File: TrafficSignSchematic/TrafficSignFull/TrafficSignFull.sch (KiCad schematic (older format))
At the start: 36 parts, among them J1 LED matrix data, J2 LED matrix power, J3 Power input, SW1 Power switch, U1 ATmega328P-PU, U2 SIM800L, U3 BQ24650 charge controller, Y1 16MHz

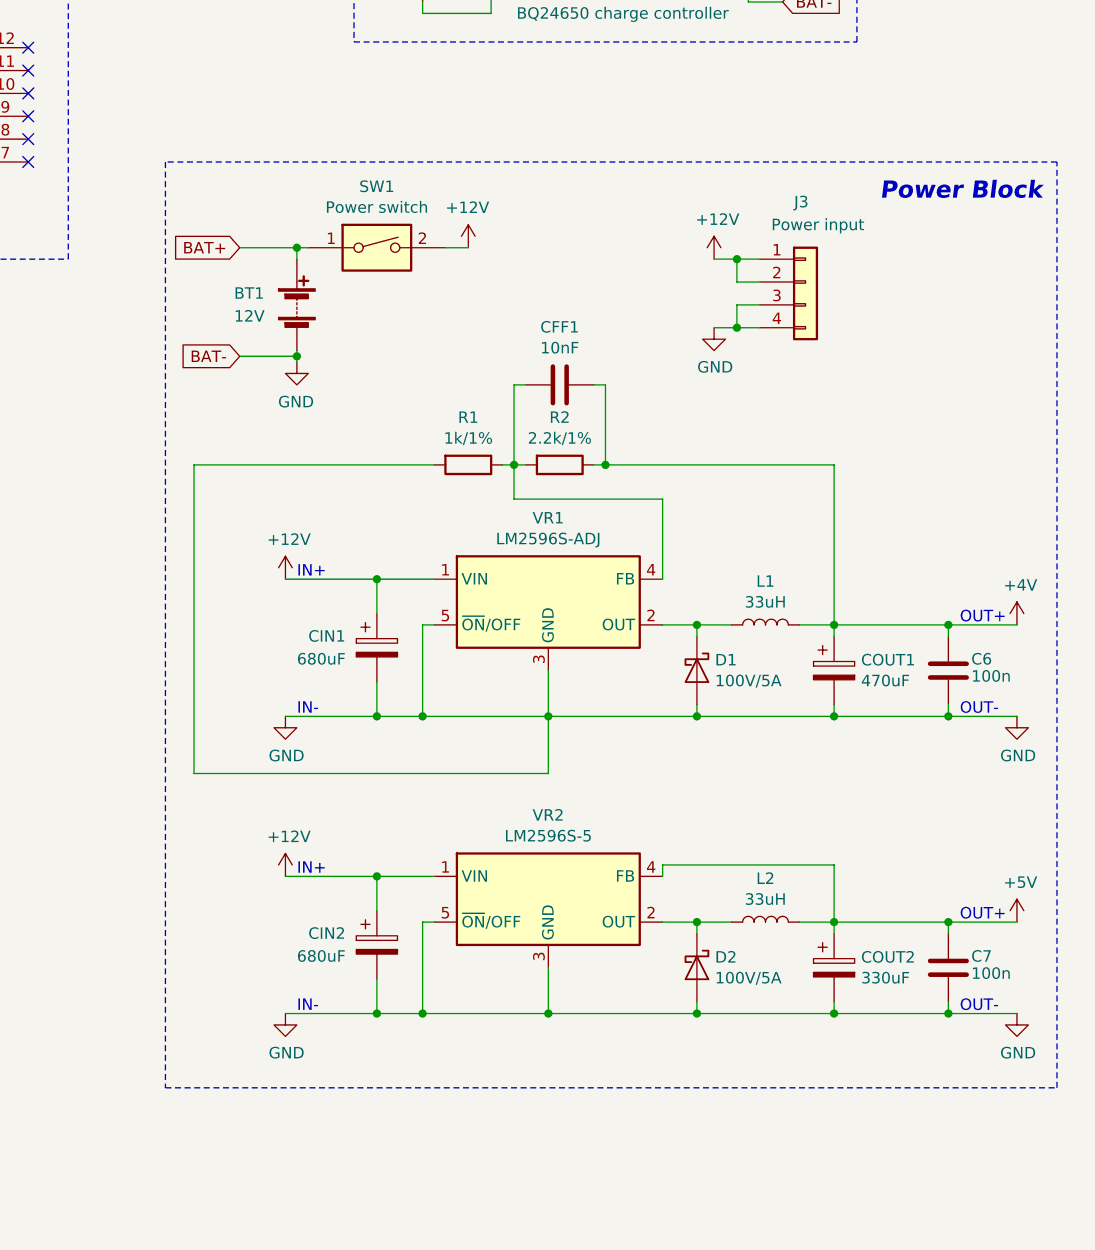
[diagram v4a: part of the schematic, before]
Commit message: Removed connector from full schematic power block
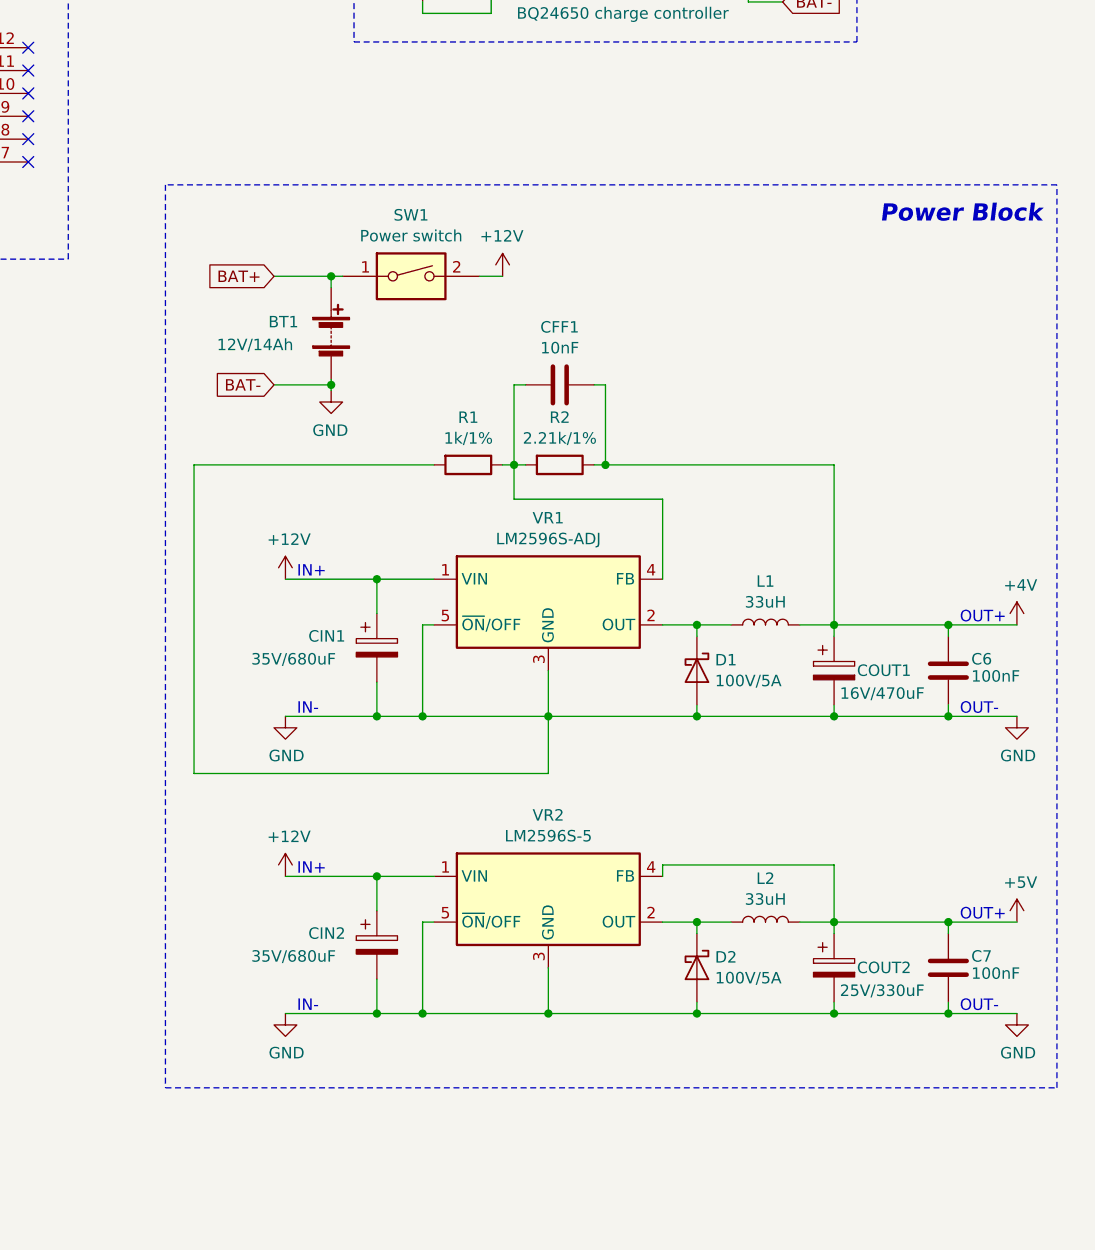
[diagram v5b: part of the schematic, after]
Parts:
- removed J3: Power input, Connector_Molex:Molex_KK-396_A-41791-0004_1x04_P3.96mm_Vertical, symbol Connector_Generic:Conn_01x04
- BT1: value 12V -> 12V/14Ah
- C6, C7: value 100n -> 100nF
- CIN1, CIN2: value 680uF -> 35V/680uF
- COUT1: value 470uF -> 16V/470uF
- COUT2: value 330uF -> 25V/330uF
- R2: value 2.2k/1% -> 2.21k/1%
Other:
- moved on the sheet: BT1, SW1
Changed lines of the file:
@@
 P 10475 5775
 F 0 "C7" H 10575 5825 50  0000 L CNN
-F 1 "100n" H 10575 5750 50  0000 L CNN
+F 1 "100nF" H 10575 5750 50  0000 L CNN
 F 2 "Capacitor_THT:C_Disc_D4.3mm_W1.9mm_P5.00mm" H 10513 5625 50  0001 C CNN
 F 3 "https://store.comet.bg/Catalogue/Product/5920/" H 10475 5775 50  0001 C CNN
@@
 P 10475 4475
 F 0 "C6" H 10575 4525 50  0000 L CNN
-F 1 "100n" H 10575 4450 50  0000 L CNN
+F 1 "100nF" H 10575 4450 50  0000 L CNN
 F 2 "Capacitor_THT:C_Disc_D4.3mm_W1.9mm_P5.00mm" H 10513 4325 50  0001 C CNN
 F 3 "https://store.comet.bg/Catalogue/Product/5920/" H 10475 4475 50  0001 C CNN
@@
 U 1 1 5DFA6ACC
 P 9975 4475
-F 0 "COUT1" H 10093 4521 50  0000 L CNN
-F 1 "470uF" H 10093 4430 50  0000 L CNN
+F 0 "COUT1" H 10075 4475 50  0000 L CNN
+F 1 "16V/470uF" H 10000 4375 50  0000 L CNN
 F 2 "Capacitor_THT:CP_Radial_D8.0mm_P3.50mm" H 10013 4325 50  0001 C CNN
 F 3 "https://store.comet.bg/Catalogue/Product/36876/" H 9975 4475 50  0001 C CNN
@@
 P 7975 5675
 F 0 "CIN2" H 7675 5725 50  0000 L CNN
-F 1 "680uF" H 7625 5625 50  0000 L CNN
+F 1 "35V/680uF" H 7425 5625 50  0000 L CNN
 F 2 "Capacitor_THT:CP_Radial_D10.0mm_P5.00mm" H 8013 5525 50  0001 C CNN
 F 3 "https://store.comet.bg/Catalogue/Product/44664/" H 7975 5675 50  0001 C CNN
@@
 U 1 1 5E2070F5
 P 9975 5775
-F 0 "COUT2" H 10093 5821 50  0000 L CNN
-F 1 "330uF" H 10093 5730 50  0000 L CNN
+F 0 "COUT2" H 10075 5775 50  0000 L CNN
+F 1 "25V/330uF" H 10000 5675 50  0000 L CNN
 F 2 "Capacitor_THT:CP_Radial_D8.0mm_P3.50mm" H 10013 5625 50  0001 C CNN
 F 3 "https://store.comet.bg/Catalogue/Product/7086/" H 9975 5775 50  0001 C CNN
@@
 Wire Wire Line
 	7575 4075 7975 4075
-Wire Wire Line
-	8575 3225 8625 3225
-Wire Wire Line
-	8575 3575 8575 3225
 Connection ~ 7975 4675
 Connection ~ 8725 4675
@@
 P 7975 4375
 F 0 "CIN1" H 7675 4425 50  0000 L CNN
-F 1 "680uF" H 7625 4325 50  0000 L CNN
+F 1 "35V/680uF" H 7425 4325 50  0000 L CNN
 F 2 "Capacitor_THT:CP_Radial_D10.0mm_P5.00mm" H 8013 4225 50  0001 C CNN
 F 3 "https://store.comet.bg/Catalogue/Product/44664/" H 7975 4375 50  0001 C CNN
@@
 P 8775 3575
 F 0 "R2" V 8568 3575 50  0000 C CNN
-F 1 "2.2k/1%" V 8659 3575 50  0000 C CNN
+F 1 "2.21k/1%" V 8659 3575 50  0000 C CNN
 F 2 "Resistor_THT:R_Axial_DIN0207_L6.3mm_D2.5mm_P10.16mm_Horizontal" V 8705 3575 50  0001 C CNN
 F 3 "https://store.comet.bg/Catalogue/Product/5041342/" H 8775 3575 50  0001 C CNN
@@
 $EndComp
 Wire Notes Line
-	7050 2250 7050 6300
-Wire Notes Line
 	7050 6300 10950 6300
 Wire Notes Line
-	10950 6300 10950 2250
-$Comp
-L Connector_Generic:Conn_01x04 J3
-U 1 1 5E26C348
-P 9850 2775
-F 0 "J3" H 9800 3125 50  0000 L CNN
-F 1 "Power input" H 9700 3025 50  0000 L CNN
-F 2 "Connector_Molex:Molex_KK-396_A-41791-0004_1x04_P3.96mm_Vertical" H 9850 2775 50  0001 C CNN
-F 3 "https://store.comet.bg/Catalogue/Product/25223/" H 9850 2775 50  0001 C CNN
-	1    9850 2775
-	1    0    0    -1
-$EndComp
-Wire Wire Line
-	9650 2675 9550 2675
-Wire Wire Line
-	9650 2775 9550 2775
-Wire Wire Line
-	9650 2875 9550 2875
-Wire Wire Line
-	9650 2975 9550 2975
-Wire Wire Line
-	9550 2875 9550 2975
-Wire Wire Line
-	9550 2975 9450 2975
-Connection ~ 9550 2975
-Wire Wire Line
-	9550 2775 9550 2675
-Wire Wire Line
-	9550 2675 9450 2675
-Connection ~ 9550 2675
-$Comp
-L power:GND #PWR0106
-U 1 1 5E43D1EE
-P 9450 2975
-F 0 "#PWR0106" H 9450 2725 50  0001 C CNN
-F 1 "GND" H 9455 2802 50  0000 C CNN
-F 2 "" H 9450 2975 50  0001 C CNN
-F 3 "" H 9450 2975 50  0001 C CNN
-	1    9450 2975
-	1    0    0    -1
-$EndComp
-$Comp
-L power:+12V #PWR0107
-U 1 1 5E463591
-P 9450 2675
-F 0 "#PWR0107" H 9450 2525 50  0001 C CNN
-F 1 "+12V" H 9465 2848 50  0000 C CNN
-F 2 "" H 9450 2675 50  0001 C CNN
-F 3 "" H 9450 2675 50  0001 C CNN
-	1    9450 2675
-	1    0    0    -1
-$EndComp
-Text Notes 10175 2425 0    75   Italic 15
+	10950 6300 10950 2350
+Text Notes 10175 2525 0    75   Italic 15
 Power Block
-Text GLabel 7375 3100 0    50   Input ~ 0
-BAT-
-Text GLabel 7375 2625 0    50   Input ~ 0
-BAT+
-Wire Wire Line
-	7625 3100 7625 3075
-Connection ~ 7625 3100
-Wire Wire Line
-	7625 3100 7375 3100
-Connection ~ 7625 2625
-Wire Wire Line
-	7625 2625 7375 2625
-Wire Notes Line
-	10950 2250 7050 2250
-Wire Wire Line
-	7625 3125 7625 3100
-$Comp
-L power:GND #PWR0124
-U 1 1 5E1818BD
-P 7625 3125
-F 0 "#PWR0124" H 7625 2875 50  0001 C CNN
-F 1 "GND" H 7700 2950 50  0000 R CNN
-F 2 "" H 7625 3125 50  0001 C CNN
-F 3 "" H 7625 3125 50  0001 C CNN
-	1    7625 3125
-	1    0    0    -1
-$EndComp
-$Comp
-L Switch:SW_DIP_x01 SW1
-U 1 1 5E329055
-P 7975 2625
-F 0 "SW1" H 7975 2892 50  0000 C CNN
-F 1 "Power switch" H 7975 2801 50  0000 C CNN
-F 2 "" H 7975 2625 50  0001 C CNN
-F 3 "~" H 7975 2625 50  0001 C CNN
-	1    7975 2625
-	1    0    0    -1
-$EndComp
-Wire Wire Line
-	8275 2625 8375 2625
-Wire Wire Line
-	7675 2625 7625 2625
-$Comp
-L power:+12V #PWR0125
-U 1 1 5E174F0C
-P 8375 2625
-F 0 "#PWR0125" H 8375 2475 50  0001 C CNN
-F 1 "+12V" H 8275 2800 50  0000 L CNN
-F 2 "" H 8375 2625 50  0001 C CNN
-F 3 "" H 8375 2625 50  0001 C CNN
-	1    8375 2625
-	1    0    0    -1
-$EndComp
-Wire Wire Line
-	7625 2625 7625 2675
-$Comp
-L Device:Battery BT1
-U 1 1 5E200195
-P 7625 2875
-F 0 "BT1" H 7350 2925 50  0000 L CNN
-F 1 "12V" H 7350 2825 50  0000 L CNN
-F 2 "" V 7625 2935 50  0001 C CNN
-F 3 "~" V 7625 2935 50  0001 C CNN
-	1    7625 2875
-	1    0    0    -1
-$EndComp
+Wire Notes Line
+	10950 2350 7050 2350
 Text GLabel 9750 1225 2    50   Input ~ 0
 BAT+
@@
 Text Notes 9275 1075 0    75   Italic 15
 Charge Block
+Text GLabel 7525 3225 0    50   Input ~ 0
+BAT-
+Text GLabel 7525 2750 0    50   Input ~ 0
+BAT+
+Wire Wire Line
+	7775 3225 7775 3200
+Connection ~ 7775 3225
+Wire Wire Line
+	7775 3225 7525 3225
+Connection ~ 7775 2750
+Wire Wire Line
+	7775 2750 7525 2750
+Wire Wire Line
+	7775 3250 7775 3225
+$Comp
+L power:GND #PWR0124
+U 1 1 5E1818BD
+P 7775 3250
+F 0 "#PWR0124" H 7775 3000 50  0001 C CNN
+F 1 "GND" H 7850 3075 50  0000 R CNN
+F 2 "" H 7775 3250 50  0001 C CNN
+F 3 "" H 7775 3250 50  0001 C CNN
+	1    7775 3250
+	1    0    0    -1
+$EndComp
+$Comp
+L Switch:SW_DIP_x01 SW1
+U 1 1 5E329055
+P 8125 2750
+F 0 "SW1" H 8125 3017 50  0000 C CNN
+F 1 "Power switch" H 8125 2926 50  0000 C CNN
+F 2 "" H 8125 2750 50  0001 C CNN
+F 3 "~" H 8125 2750 50  0001 C CNN
+	1    8125 2750
+	1    0    0    -1
+$EndComp
+Wire Wire Line
+	8425 2750 8525 2750
+Wire Wire Line
+	7825 2750 7775 2750
+$Comp
+L power:+12V #PWR0125
+U 1 1 5E174F0C
+P 8525 2750
+F 0 "#PWR0125" H 8525 2600 50  0001 C CNN
+F 1 "+12V" H 8425 2925 50  0000 L CNN
+F 2 "" H 8525 2750 50  0001 C CNN
+F 3 "" H 8525 2750 50  0001 C CNN
+	1    8525 2750
+	1    0    0    -1
+$EndComp
+Wire Wire Line
+	7775 2750 7775 2800
+$Comp
+L Device:Battery BT1
+U 1 1 5E200195
+P 7775 3000
+F 0 "BT1" H 7500 3050 50  0000 L CNN
+F 1 "12V/14Ah" H 7275 2950 50  0000 L CNN
+F 2 "" V 7775 3060 50  0001 C CNN
+F 3 "~" V 7775 3060 50  0001 C CNN
+	1    7775 3000
+	1    0    0    -1
+$EndComp
+Wire Wire Line
+	8575 3575 8575 3225
+Wire Wire Line
+	8575 3225 8625 3225
+Wire Notes Line
+	7050 2350 7050 6300
 $EndSCHEMATC

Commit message: Added an aditional voltage divider
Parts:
- added R8: 20k, Resistor_THT:R_Axial_DIN0204_L3.6mm_D1.6mm_P7.62mm_Horizontal, symbol Device:R
- R7: value 10k -> 16k
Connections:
- net GND: now also R8.2
- net at R7.2, U2.3 (RST): now also R8.1
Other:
- moved on the sheet: AE1, R3, R4, R6, U2
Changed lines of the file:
@@
 encoding utf-8
 Sheet 1 1
-Title ""
-Date ""
-Rev ""
+Title "Full traffic sign schematic"
+Date "2020-02-15"
+Rev "1"
 Comp ""
 Comment1 ""
@@
 Text GLabel 4725 6600 2    50   Input ~ 0
 SIM_RST
-Text GLabel 4750 1900 0    50   Input ~ 0
+Text GLabel 4425 1100 0    50   Input ~ 0
 SIM_RST
 Wire Wire Line
-	5175 2100 5200 2100
+	5175 2150 5200 2150
 Wire Wire Line
 	2550 4550 2700 4550
@@
 $EndComp
 Wire Wire Line
-	5050 1800 5200 1800
+	5050 1850 5200 1850
 $Comp
 L power:+4V #PWR0117
 U 1 1 5E526B11
-P 5050 1800
-F 0 "#PWR0117" H 5050 1650 50  0001 C CNN
-F 1 "+4V" H 5050 1950 50  0000 C CNN
-F 2 "" H 5050 1800 50  0001 C CNN
-F 3 "" H 5050 1800 50  0001 C CNN
-	1    5050 1800
-	1    0    0    -1
-$EndComp
-$Comp
-L power:GND #PWR0116
-U 1 1 5E4EA9BE
-P 4175 2400
-F 0 "#PWR0116" H 4175 2150 50  0001 C CNN
-F 1 "GND" H 4175 2250 50  0000 C CNN
-F 2 "" H 4175 2400 50  0001 C CNN
-F 3 "" H 4175 2400 50  0001 C CNN
-	1    4175 2400
+P 5050 1850
+F 0 "#PWR0117" H 5050 1700 50  0001 C CNN
+F 1 "+4V" H 5050 2000 50  0000 C CNN
+F 2 "" H 5050 1850 50  0001 C CNN
+F 3 "" H 5050 1850 50  0001 C CNN
+	1    5050 1850
 	1    0    0    -1
 $EndComp
@@
 L Device:R R3
 U 1 1 5E100EA7
-P 4175 1800
-F 0 "R3" H 4225 1850 50  0000 L CNN
-F 1 "16k" H 4225 1775 50  0000 L CNN
-F 2 "Resistor_THT:R_Axial_DIN0204_L3.6mm_D1.6mm_P7.62mm_Horizontal" V 4105 1800 50  0001 C CNN
-F 3 "https://store.comet.bg/Catalogue/Product/25851/" H 4175 1800 50  0001 C CNN
-	1    4175 1800
-	1    0    0    -1
-$EndComp
-Wire Wire Line
-	4100 1650 4175 1650
+P 4175 1850
+F 0 "R3" H 4225 1900 50  0000 L CNN
+F 1 "16k" H 4225 1825 50  0000 L CNN
+F 2 "Resistor_THT:R_Axial_DIN0204_L3.6mm_D1.6mm_P7.62mm_Horizontal" V 4105 1850 50  0001 C CNN
+F 3 "https://store.comet.bg/Catalogue/Product/25851/" H 4175 1850 50  0001 C CNN
+	1    4175 1850
+	1    0    0    -1
+$EndComp
+Wire Wire Line
+	4100 1700 4175 1700
 Wire Wire Line
 	4505 5000 4620 5000
@@
 L Device:R R4
 U 1 1 5E2884D8
-P 4175 2200
-F 0 "R4" H 4225 2250 50  0000 L CNN
-F 1 "20k" H 4225 2175 50  0000 L CNN
-F 2 "Resistor_THT:R_Axial_DIN0204_L3.6mm_D1.6mm_P7.62mm_Horizontal" V 4105 2200 50  0001 C CNN
-F 3 "https://store.comet.bg/Catalogue/Product/3884/" H 4175 2200 50  0001 C CNN
-	1    4175 2200
-	1    0    0    -1
-$EndComp
-Wire Wire Line
-	4175 2400 4175 2350
+P 4175 2250
+F 0 "R4" H 4225 2300 50  0000 L CNN
+F 1 "20k" H 4225 2225 50  0000 L CNN
+F 2 "Resistor_THT:R_Axial_DIN0204_L3.6mm_D1.6mm_P7.62mm_Horizontal" V 4105 2250 50  0001 C CNN
+F 3 "https://store.comet.bg/Catalogue/Product/3884/" H 4175 2250 50  0001 C CNN
+	1    4175 2250
+	1    0    0    -1
+$EndComp
 $Comp
 L Device:C C2
@@
 L TrafficSignPCB-rescue:SIM800L-SIM800L U2
 U 1 1 5DF831F1
-P 5800 2000
-F 0 "U2" H 5500 2600 60  0000 C CNN
-F 1 "SIM800L" H 5600 2500 60  0000 C CNN
-F 2 "SIM800:Sim800L" H 6100 1850 60  0001 C CNN
-F 3 "https://img.filipeflop.com/files/download/Datasheet_SIM800L.pdf" H 6100 1850 60  0001 C CNN
-	1    5800 2000
-	1    0    0    -1
-$EndComp
-NoConn ~ 6450 2250
-NoConn ~ 6450 2150
-NoConn ~ 6450 2050
-NoConn ~ 6450 1950
-NoConn ~ 6450 1850
-NoConn ~ 6450 1750
+P 5800 2050
+F 0 "U2" H 5500 2650 60  0000 C CNN
+F 1 "SIM800L" H 5600 2550 60  0000 C CNN
+F 2 "SIM800:Sim800L" H 6100 1900 60  0001 C CNN
+F 3 "https://img.filipeflop.com/files/download/Datasheet_SIM800L.pdf" H 6100 1900 60  0001 C CNN
+	1    5800 2050
+	1    0    0    -1
+$EndComp
+NoConn ~ 6450 2300
+NoConn ~ 6450 2200
+NoConn ~ 6450 2100
+NoConn ~ 6450 2000
+NoConn ~ 6450 1900
+NoConn ~ 6450 1800
 $Comp
 L Device:R R2
@@
 	4125 4700 4725 4700
 Wire Wire Line
-	5175 1900 5200 1900
-Wire Wire Line
-	4875 1900 4750 1900
-Wire Wire Line
-	5050 2200 5200 2200
+	5050 2250 5200 2250
 $Comp
 L power:GND #PWR0118
 U 1 1 5E53B52D
-P 5050 2200
-F 0 "#PWR0118" H 5050 1950 50  0001 C CNN
-F 1 "GND" H 5050 2050 50  0000 C CNN
-F 2 "" H 5050 2200 50  0001 C CNN
-F 3 "" H 5050 2200 50  0001 C CNN
-	1    5050 2200
-	1    0    0    -1
-$EndComp
-Wire Wire Line
-	4875 2100 4750 2100
-Text GLabel 4750 2100 0    50   Input ~ 0
+P 5050 2250
+F 0 "#PWR0118" H 5050 2000 50  0001 C CNN
+F 1 "GND" H 5050 2100 50  0000 C CNN
+F 2 "" H 5050 2250 50  0001 C CNN
+F 3 "" H 5050 2250 50  0001 C CNN
+	1    5050 2250
+	1    0    0    -1
+$EndComp
+Wire Wire Line
+	4875 2150 4750 2150
+Text GLabel 4750 2150 0    50   Input ~ 0
 SIM_TX
-Text GLabel 4100 1650 0    50   Input ~ 0
+Text GLabel 4100 1700 0    50   Input ~ 0
 SIM_RX
 Wire Wire Line
-	4175 2000 5200 2000
-Connection ~ 4175 2000
+	4175 2050 5200 2050
+Connection ~ 4175 2050
+Wire Wire Line
+	4175 2050 4175 2100
 Wire Wire Line
 	4175 2000 4175 2050
-Wire Wire Line
-	4175 1950 4175 2000
 Wire Notes Line
 	1000 875  3200 875
@@
 L Device:R R6
 U 1 1 5E6F86C9
-P 5025 2100
-F 0 "R6" V 5060 2280 50  0000 C CNN
-F 1 "10k" V 4980 2280 50  0000 C CNN
-F 2 "Resistor_THT:R_Axial_DIN0204_L3.6mm_D1.6mm_P7.62mm_Horizontal" V 4955 2100 50  0001 C CNN
-F 3 "~" H 5025 2100 50  0001 C CNN
-	1    5025 2100
-	0    -1   -1   0
-$EndComp
-$Comp
-L Device:R R7
-U 1 1 5E295091
-P 5025 1900
-F 0 "R7" V 5060 2080 50  0000 C CNN
-F 1 "10k" V 4980 2080 50  0000 C CNN
-F 2 "Resistor_THT:R_Axial_DIN0204_L3.6mm_D1.6mm_P7.62mm_Horizontal" V 4955 1900 50  0001 C CNN
-F 3 "~" H 5025 1900 50  0001 C CNN
-	1    5025 1900
+P 5025 2150
+F 0 "R6" V 5060 2330 50  0000 C CNN
+F 1 "10k" V 4980 2330 50  0000 C CNN
+F 2 "Resistor_THT:R_Axial_DIN0204_L3.6mm_D1.6mm_P7.62mm_Horizontal" V 4955 2150 50  0001 C CNN
+F 3 "~" H 5025 2150 50  0001 C CNN
+	1    5025 2150
 	0    -1   -1   0
 $EndComp
@@
 $EndComp
 Wire Notes Line
-	3725 1025 3725 2675
+	3725 975  3725 2675
 Wire Notes Line
 	3725 2675 6625 2675
 Wire Notes Line
-	6625 2675 6625 1025
-Wire Notes Line
-	6625 1025 3725 1025
-Text Notes 5350 1175 0    75   Italic 15
+	6625 2675 6625 975
+Wire Notes Line
+	6625 975  3725 975
+Text Notes 5350 1125 0    75   Italic 15
 Communication Block
 Wire Wire Line
-	5175 1700 5200 1700
-Wire Wire Line
-	5175 1600 5175 1700
+	5175 1750 5200 1750
+Wire Wire Line
+	5175 1650 5175 1750
 $Comp
 L Device:Antenna AE1
 U 1 1 5E0362F2
-P 5175 1400
-F 0 "AE1" H 5100 1650 50  0000 L CNN
-F 1 "Antenna" H 5025 1550 50  0000 L CNN
-F 2 "Connector_Coaxial:SMA_Amphenol_901-144_Vertical" H 5175 1400 50  0001 C CNN
-F 3 "https://store.comet.bg/Catalogue/Product/51344/" H 5175 1400 50  0001 C CNN
-	1    5175 1400
+P 5175 1450
+F 0 "AE1" H 5100 1700 50  0000 L CNN
+F 1 "Antenna" H 5025 1600 50  0000 L CNN
+F 2 "Connector_Coaxial:SMA_Amphenol_901-144_Vertical" H 5175 1450 50  0001 C CNN
+F 3 "https://store.comet.bg/Catalogue/Product/51344/" H 5175 1450 50  0001 C CNN
+	1    5175 1450
 	1    0    0    -1
 $EndComp
@@
 Wire Notes Line
 	7050 2350 7050 6300
+$Comp
+L Device:R R7
+U 1 1 5E490DB1
+P 4500 1250
+F 0 "R7" H 4550 1300 50  0000 L CNN
+F 1 "16k" H 4550 1225 50  0000 L CNN
+F 2 "Resistor_THT:R_Axial_DIN0204_L3.6mm_D1.6mm_P7.62mm_Horizontal" V 4430 1250 50  0001 C CNN
+F 3 "https://store.comet.bg/Catalogue/Product/25851/" H 4500 1250 50  0001 C CNN
+	1    4500 1250
+	1    0    0    -1
+$EndComp
+Wire Wire Line
+	4425 1100 4500 1100
+$Comp
+L Device:R R8
+U 1 1 5E490DB8
+P 4500 1650
+F 0 "R8" H 4550 1700 50  0000 L CNN
+F 1 "20k" H 4550 1625 50  0000 L CNN
+F 2 "Resistor_THT:R_Axial_DIN0204_L3.6mm_D1.6mm_P7.62mm_Horizontal" V 4430 1650 50  0001 C CNN
+F 3 "https://store.comet.bg/Catalogue/Product/3884/" H 4500 1650 50  0001 C CNN
+	1    4500 1650
+	1    0    0    -1
+$EndComp
+Wire Wire Line
+	4500 1400 4500 1450
+Wire Wire Line
+	4750 1450 4500 1450
+Connection ~ 4500 1450
+Wire Wire Line
+	4500 1450 4500 1500
+Wire Wire Line
+	4750 1950 5200 1950
+Wire Wire Line
+	4175 2450 4175 2400
+$Comp
+L power:GND #PWR0116
+U 1 1 5E4EA9BE
+P 4175 2450
+F 0 "#PWR0116" H 4175 2200 50  0001 C CNN
+F 1 "GND" H 4175 2300 50  0000 C CNN
+F 2 "" H 4175 2450 50  0001 C CNN
+F 3 "" H 4175 2450 50  0001 C CNN
+	1    4175 2450
+	1    0    0    -1
+$EndComp
+Wire Wire Line
+	4500 1850 4500 1800
+$Comp
+L power:GND #PWR0106
+U 1 1 5E490DAB
+P 4500 1850
+F 0 "#PWR0106" H 4500 1600 50  0001 C CNN
+F 1 "GND" H 4500 1700 50  0000 C CNN
+F 2 "" H 4500 1850 50  0001 C CNN
+F 3 "" H 4500 1850 50  0001 C CNN
+	1    4500 1850
+	1    0    0    -1
+$EndComp
+Wire Wire Line
+	4750 1450 4750 1950
 $EndSCHEMATC
